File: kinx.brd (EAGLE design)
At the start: 122 x 86 mm, 45 parts, among them T1 MCP1825S

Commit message: better net names
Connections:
- net N$11 renamed PTA2
- net N$29 renamed USBFS_VBUS
- net N$30 renamed PTA1
- net N$8 renamed USBHS_VBUS
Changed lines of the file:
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@@
 <wire x1="21" y1="67.1" x2="29" y2="67.1" width="0.35" layer="16"/>
 </signal>
-<signal name="N$29" class="2">
+<signal name="USBFS_VBUS" class="2">
 <contactref element="C3" pad="1"/>
 <contactref element="R12" pad="1"/>
@@
 <wire x1="26.25" y1="59.5125625" x2="25.2624375" y2="58.525" width="0.4" layer="16"/>
 </signal>
-<signal name="N$30">
+<signal name="PTA1">
 <contactref element="MKL04Z32VLC4" pad="10"/>
 <contactref element="U$1" pad="51"/>
@@
 <wire x1="68.762" y1="36.1" x2="70.933" y2="36.107" width="0.4" layer="16"/>
 </signal>
-<signal name="N$11">
+<signal name="PTA2">
 <contactref element="MKL04Z32VLC4" pad="17"/>
 <contactref element="U$1" pad="52"/>
@@
 <wire x1="91.46" y1="42.54" x2="89" y2="45" width="0.2" layer="16"/>
 </signal>
-<signal name="N$8">
+<signal name="USBHS_VBUS">
 <contactref element="USBHS" pad="1"/>
 <contactref element="U$1" pad="27"/>

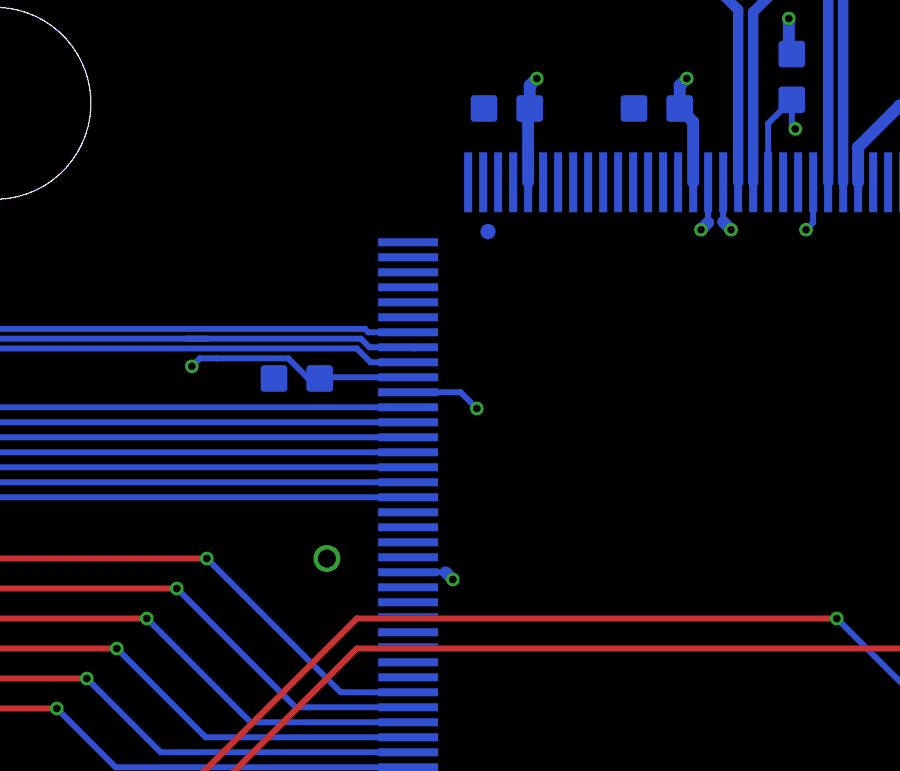
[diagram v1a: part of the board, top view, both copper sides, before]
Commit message: Increase isolation of GND planes for better manufacturability
Done using “change isolate 8mil” on both GND planes.

A few previous PCBs had their ground plane accidentally connected to traces.

OSH Park explained that this can be due to imbalances in the acid concentration,
and advised to increase isolation.
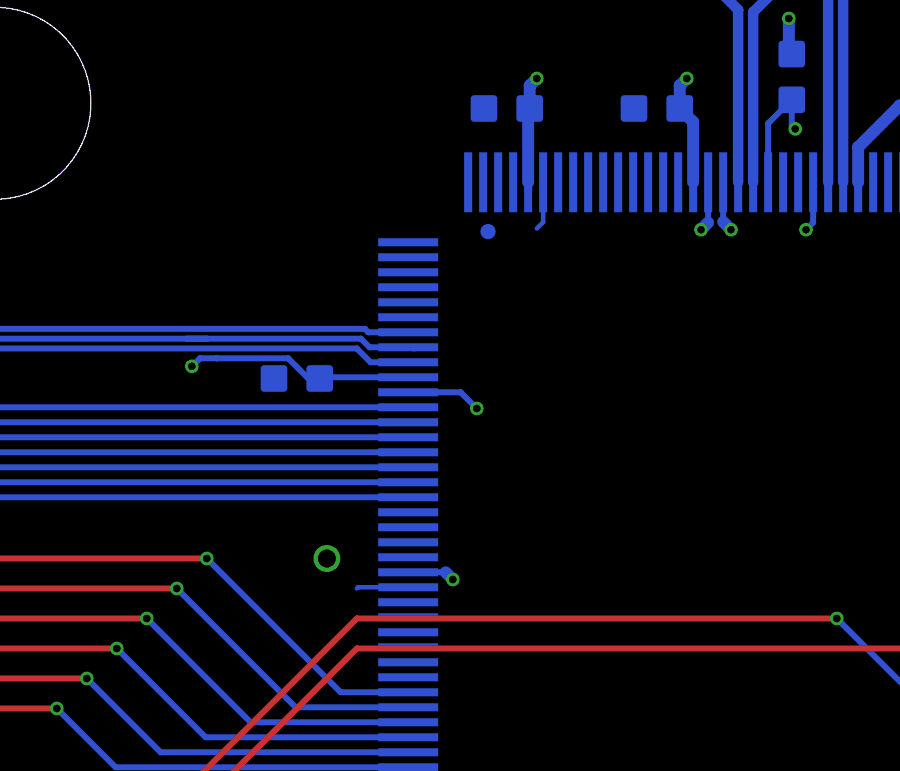
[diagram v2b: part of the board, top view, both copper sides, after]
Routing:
- net GND: track 39.9 -> 43.3 mm
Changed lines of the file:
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@@
 <signals>
 <signal name="GND">
-<polygon width="0.4064" layer="1">
+<polygon width="0.4064" layer="1" isolate="0.2032">
 <vertex x="1" y="85"/>
 <vertex x="1" y="1"/>
@@
 <contactref element="USBHS" pad="P$1"/>
 <contactref element="USBHS" pad="P$2"/>
-<polygon width="0.4064" layer="16">
+<polygon width="0.4064" layer="16" isolate="0.2032">
 <vertex x="1" y="85"/>
 <vertex x="1" y="1"/>
@@
 <wire x1="24.35" y1="60.9" x2="23.972" y2="61.278" width="0.4" layer="16"/>
 <wire x1="23.972" y1="61.278" x2="23.972" y2="62.06" width="0.4" layer="16"/>
+<wire x1="74.71" y1="46.04" x2="73.04" y2="46.04" width="0.1524" layer="16"/>
+<wire x1="73.04" y1="46.04" x2="73" y2="46" width="0.1524" layer="16"/>
+<wire x1="79.21" y1="59.54" x2="79.21" y2="58.21" width="0.1524" layer="16"/>
+<wire x1="79.21" y1="58.21" x2="79" y2="58" width="0.1524" layer="16"/>
 </signal>
 <signal name="N$12">
